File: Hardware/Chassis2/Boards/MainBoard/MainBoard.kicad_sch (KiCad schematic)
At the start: 28 parts, among them J1 Conn_02x08_Counter_Clockwise, J11 Conn_02x10_Counter_Clockwise, J12 Conn_02x10_Counter_Clockwise, J13 Conn_02x10_Counter_Clockwise, J14 Conn_02x10_Counter_Clockwise, J2 Conn_02x08_Counter_Clockwise, J3 Conn_02x08_Counter_Clockwise, J4 TBP01R1-508-06BE, J5 Conn_02x10_Counter_Clockwise, J6 TBP01R2-508-06BE

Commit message: Added New Control Board
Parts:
- removed C148, C149, C150, C151, C152, C153, C154, C155, C156, C157, C158, C159: UCM1H101MCL1GS, InverterCom:CAPAE660X800N, symbol InverterCom:UCM1H101MCL1GS
- removed H1, H7: MountingHole, MountingHole:MountingHole_3.2mm_M3, symbol Mechanical:MountingHole
- removed H3, H4, H5, H8: MountingHole, MountingHole:MountingHole_4.3mm_M4, symbol Mechanical:MountingHole
- removed J1, J2, J3: Conn_02x08_Counter_Clockwise, Connector_PinSocket_2.54mm:PinSocket_2x08_P2.54mm_Vertical, symbol Connector_Generic:Conn_02x08_Counter_Clockwise
- removed J11, J12, J13, J14, J5: Conn_02x10_Counter_Clockwise, Connector_PinHeader_2.54mm:PinHeader_2x10_P2.54mm_Vertical, symbol Connector_Generic:Conn_02x10_Counter_Clockwise
- removed J4: TBP01R1-508-06BE, InverterCom:TBP01R150806BE, symbol InverterCom:TBP01R1-508-06BE
- removed J6: TBP01R2-508-06BE, InverterCom:TBP01R250806BE, symbol InverterCom:TBP01R2-508-06BE
- added D3, D4: S3N, InverterCom:DIOM8059X265N, symbol InverterCom:S3N
- added F1: MF-RHT200_32-2, InverterCom:MFRHT200322, symbol InverterCom:MF-RHT200_32-2
- added J6: 776231-1, 7762311, symbol InverterCom:776231-1
- added PS3: EC7BW-110S12, EC7BW110S12, symbol InverterCom:EC7BW-110S12
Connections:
- net CAN_HIGH: now also J6.16
- net CAN_JUMPER_A: now also J6.2
- net CAN_LOW: now also J6.24, J6.27
- net GND_A: now also J6.15, PS3.5 (-VOUT)
- new net: D3.2 (A), D4.2 (A), F1.2
- new net +12V_OUT_A: PS3.3 (+VOUT)
- new net +5V_A: J6.26
- new net DIGITAL_IN_1: J6.18
- new net DIGITAL_IN_2: J6.30
- new net DIGITAL_IN_8: J6.21
- new net GND_Z: PS3.2 (-VIN)
- new net MOTOR_TMP_SENSE_IN: J6.33
- new net THROTTLE_A_IN: J6.22
- new net THROTTLE_B_IN: J6.23
- new net VIN_FUSED_Z: D3.1 (K), D4.1 (K), PS3.1 (+VIN)
- new net VIN_Z: F1.1, J6.1, J6.6
- no-connect marks 0 -> 20
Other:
- removed sheet ADC_1
- removed sheet CAN
- removed sheet OutputRelays
- note added: "+12V POWER SUPPLY 15W MAX"
- note added: "INPUT POLARITY PROTECTION"
- note added: "VIN IS 9-18V ONLY"
- note removed: "CANBUS OUTPUT CONNECTOR TO CONTROL BOARD INTERFACES TO OUTSIDE WORLD"
- note removed: "CONNECTION FROM MAINBOARD TO CONTROL MODULE ABOVE PROVIDES RELAY OUTPUTS + GATE DRIVER INTERLOCK"
- note removed: "CONNECTOR FROM MAIN BOARD TO CONTROL MODULE ABOVE ADC SPI INPUTS / POWER TO ADCS"
- note removed: "CONNECTOR FROM MAIN BOARD TO CONTROL MODULE ABOVE ADC SPI INPUTS / POWER TO ADCS / GATE DRIVE SIGNALS"
- note removed: "CONNECTOR FROM MAIN BOARD TO CONTROL MODULE ABOVE CONTROL INPUTS + POWER TO RELAY SUBSYSTEM/GATE DRIVERS"
- note removed: "CONNECTOR FROM THIS CONTROL BOARD TO GATE DRIVER ABOVE"

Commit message: Finished New Control Board, Did Schematic For Interface Board
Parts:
- added J1: TBP01R2W-508-06BE, SHDR6W100P0X508_1X6_4064X850X1240P, symbol InverterCom:TBP01R2W-508-06BE
- added J10, J13: Conn_02x03_Counter_Clockwise, Connector_PinHeader_2.54mm:PinHeader_2x03_P2.54mm_Vertical, symbol Connector_Generic:Conn_02x03_Counter_Clockwise
- added J12, J7: Conn_02x08_Counter_Clockwise, Connector_PinHeader_2.54mm:PinHeader_2x08_P2.54mm_Vertical, symbol Connector_Generic:Conn_02x08_Counter_Clockwise
- added J14: Conn_01x10, Connector_PinHeader_2.54mm:PinHeader_1x10_P2.54mm_Vertical, symbol Connector_Generic:Conn_01x10
- added J2: Conn_01x02, Connector_PinHeader_2.54mm:PinHeader_1x02_P2.54mm_Vertical, symbol Connector_Generic:Conn_01x02
- added R1, R3, R4, R5, R6, R82: 47k, Resistor_SMD:R_1210_3225Metric_Pad1.30x2.65mm_HandSolder, symbol Device:R
- added R2, R7: 10k, Resistor_SMD:R_1210_3225Metric_Pad1.30x2.65mm_HandSolder, symbol Device:R
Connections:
- net +12V_OUT_A: now also J2.1 (Pin_1)
- net +5V_A: now also J7.16 (Pin_16)
- net CAN_JUMPER_B: now also J6.24
- net DIGITAL_IN_1: now also R3.2
- net DIGITAL_IN_2: now also R4.2
- net GND_A: now also J2.2 (Pin_2), J7.10 (Pin_10), J7.12 (Pin_12), J7.13 (Pin_13), J7.14 (Pin_14), J7.15 (Pin_15), J7.2 (Pin_2), J7.4 (Pin_4), J7.6 (Pin_6), J7.8 (Pin_8)
- net GND_Z: now also J1.1, R6.1, R82.1
- net THROTTLE_A_IN: now also J7.9 (Pin_9)
- net THROTTLE_B_IN: now also J7.11 (Pin_11)
- net VIN_Z: now also R1.2, R5.2
- net CAN1_+5V: now reaches J6.28
- net CAN1_+5V: now also J10.3 (Pin_3)
- net ENCODER_COS: now reaches J6.35
- net ENCODER_COS: now also J7.3 (Pin_3)
- net CAN_HIGH renamed CAN1_HIGH
- net CAN1_HIGH: now also J10.6 (Pin_6)
- net CAN_LOW renamed CAN1_LOW
- net CAN1_LOW: now also J10.5 (Pin_5); no longer J6.24
- net DIGITAL_IN_8 renamed ENCODER_SIN
- net ENCODER_SIN: now also J7.1 (Pin_1)
- net MOTOR_TMP_SENSE_IN renamed MOTOR_TEMP_IN
- net MOTOR_TEMP_IN: now also J7.7 (Pin_7)
- new net: R4.1, R5.1, R6.2, R7.2
- new net: R1.1, R2.2, R3.1, R82.2
- new net CAN1_GND: J10.4 (Pin_4)
- new net CAN1_JUMPER_A: J10.1 (Pin_1)
- new net CAN1_JUMPER_B: J10.2 (Pin_2)
- new net CAN2_+5V: J1.6, J13.3 (Pin_3)
- new net CAN2_GND: J1.3, J13.4 (Pin_4)
- new net CAN2_HIGH: J1.5, J13.6 (Pin_6)
- new net CAN2_JUMPER_A: J13.1 (Pin_1)
- new net CAN2_JUMPER_B: J13.2 (Pin_2)
- new net CAN2_LOW: J1.4, J13.5 (Pin_5)
- new net DIN_1_W: J12.1 (Pin_1), R2.1
- new net DIN_2_W: J12.3 (Pin_3), R7.1
- new net DIN_3_W: J12.5 (Pin_5)
- new net DIN_4_W: J12.7 (Pin_7)
- new net DIN_5_W: J12.9 (Pin_9)
- new net DIN_6_W: J12.11 (Pin_11)
- new net DIN_7_W: J12.13 (Pin_13)
- new net DIN_8_W: J12.15 (Pin_15)
- new net GND_W: J12.10 (Pin_10), J12.12 (Pin_12), J12.14 (Pin_14), J12.16 (Pin_16), J12.2 (Pin_2), J12.4 (Pin_4), J12.6 (Pin_6), J12.8 (Pin_8)
- new net HALL_W_IN: J7.5 (Pin_5)
- no-connect marks 20 -> 36
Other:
- note added: "CONNECT PIN 1 TO BATT- WHEN RUNNING FOR REAL"
- note added: "Connector to IO board"
- note added: "SINGLE WIRE DEBUG / PROGRAMMING"
- note added: "passthrough, leave above board below, we can simply add a female to male header with long pins here to make probing easier"
- note added: "power out to board below us"
- note added: "vdivs for digital inputs"
- note removed: "+12V POWER SUPPLY 15W MAX"
- note removed: "VIN IS 9-18V ONLY"
- moved on the sheet: J6

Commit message: Add New Mainboard
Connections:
- net GND_W: now also J1.2
- no-connect marks 36 -> 35
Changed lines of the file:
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@@
-	)
-	(no_connect
-		(at 151.13 30.48)
 	)
 	(no_connect
@@
 		(effects
 			(font
+				(size 1.27 1.27)
+			)
+			(justify right bottom)
+		)
+	)
+	(label "GND_W"
+		(at 151.13 30.48 270)
+		(effects
+			(font

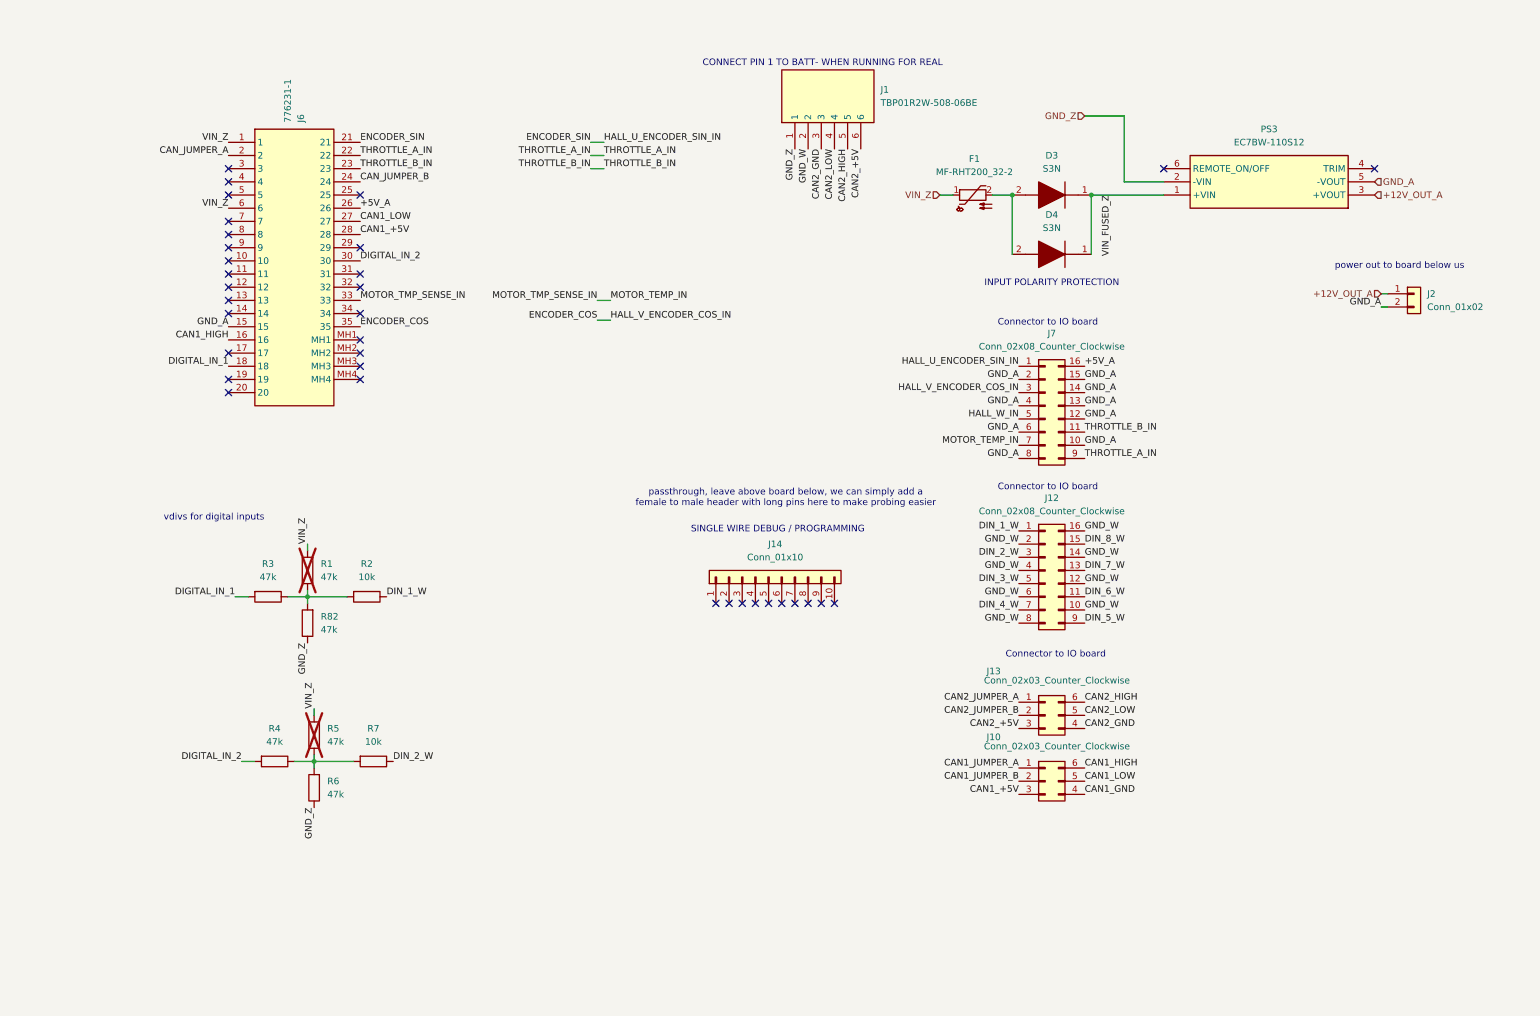
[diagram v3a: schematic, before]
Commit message: Update Inverter design for powertrain integration
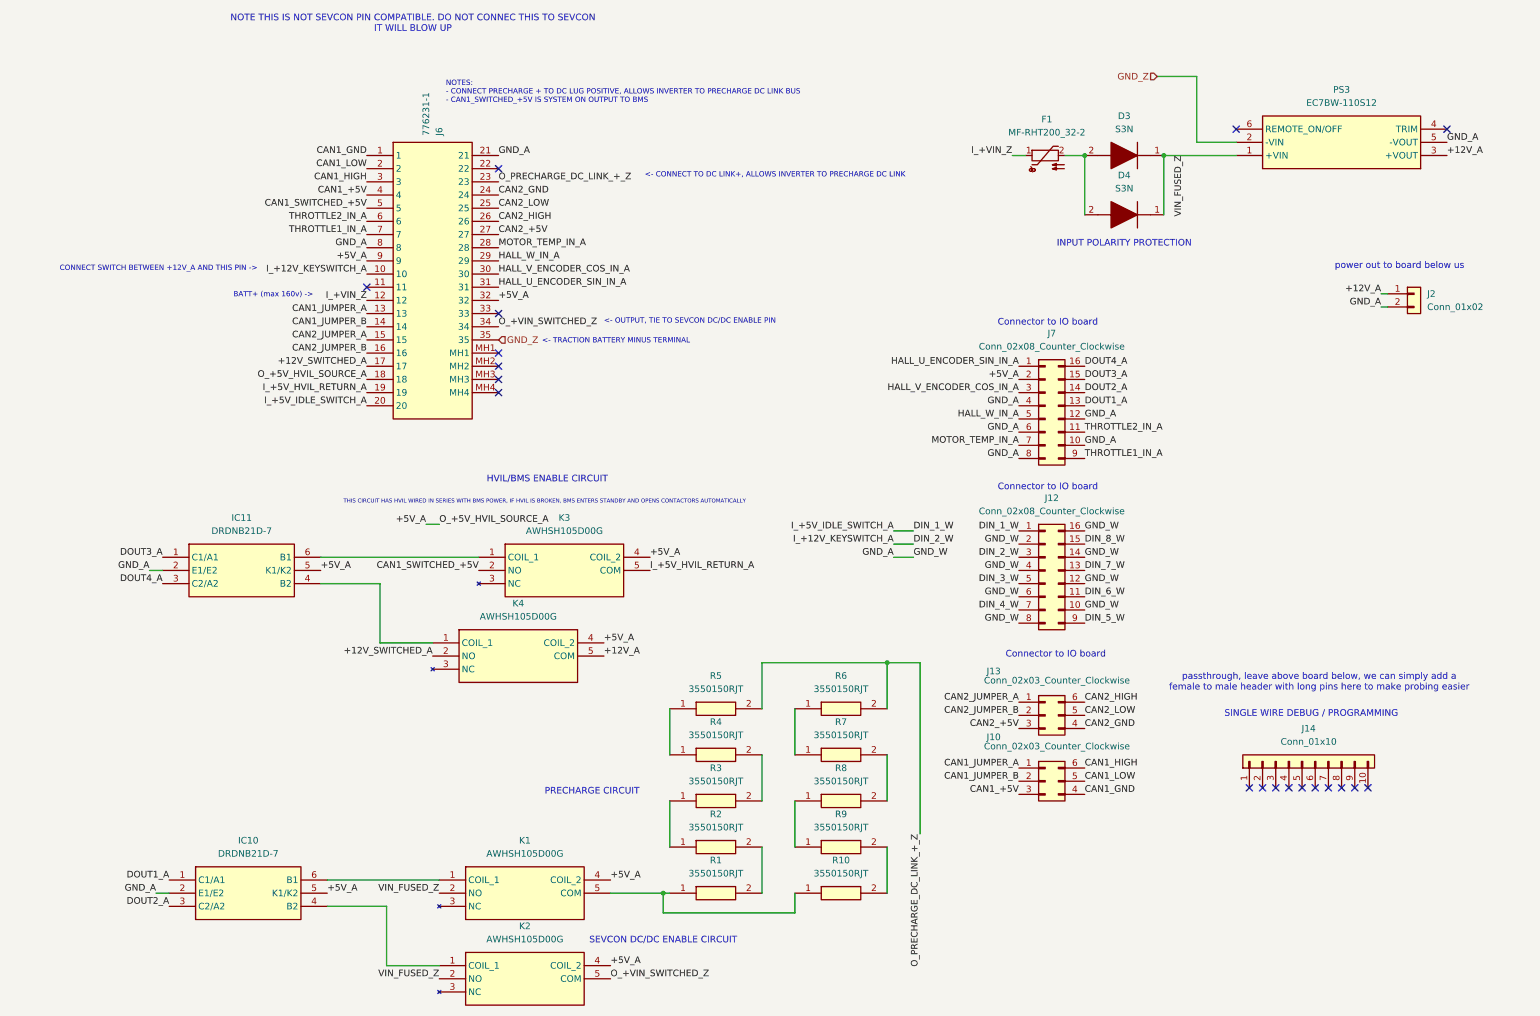
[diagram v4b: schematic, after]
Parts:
- removed J1: TBP01R2W-508-06BE, SHDR6W100P0X508_1X6_4064X850X1240P, symbol InverterCom:TBP01R2W-508-06BE
- removed R1, R3, R4, R5, R6, R82: 47k, Resistor_SMD:R_1210_3225Metric_Pad1.30x2.65mm_HandSolder, symbol Device:R
- removed R2, R7: 10k, Resistor_SMD:R_1210_3225Metric_Pad1.30x2.65mm_HandSolder, symbol Device:R
- added IC10, IC11: DRDNB21D-7, InverterCom:SOT65P210X110-6N, symbol InverterCom:DRDNB21D-7
- added K1, K2, K3, K4: AWHSH105D00G, InverterCom:AWHSH105D00G, symbol InverterCom:AWHSH105D00G
- added R1, R10, R2, R3, R4, R5, R6, R7, R8, R9: 3550150RJT, RESC11050X120N, symbol InverterCom:3550150RJT
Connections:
- net CAN_JUMPER_A is gone; now on net CAN1_LOW: J6.2
- net CAN_JUMPER_B is gone; now on net CAN2_GND: J6.24
- net DIGITAL_IN_1 is gone; now on net +5V_A: J6.18
- net GND_W is gone; now on net GND_A: J12.10 (Pin_10), J12.12 (Pin_12), J12.14 (Pin_14), J12.16 (Pin_16), J12.2 (Pin_2), J12.4 (Pin_4), J12.6 (Pin_6), J12.8 (Pin_8)
- net HALL_W_IN is gone; now on net HALL_W_IN_A: J7.5 (Pin_5)
- net +5V_A: now also J6.32, J6.9, J7.2 (Pin_2), IC10.5 (K1/K2), IC11.5 (K1/K2), K1.4 (COIL_2), K2.4 (COIL_2), K3.4 (COIL_2), K4.4 (COIL_2); no longer J6.26, J7.16 (Pin_16)
- net CAN1_+5V: now also J6.4; no longer J6.28
- net CAN1_GND: now also J6.1
- net CAN1_HIGH: now also J6.3; no longer J6.16
- net CAN1_JUMPER_A: now also J6.13
- net CAN1_JUMPER_B: now also J6.14
- net CAN1_LOW: no longer J6.27
- net CAN2_+5V: now also J6.27
- net CAN2_HIGH: now also J6.26
- net CAN2_JUMPER_A: now also J6.15
- net CAN2_JUMPER_B: now also J6.16
- net CAN2_LOW: now also J6.25
- net DIN_1_W: now also J6.20
- net DIN_2_W: now also J6.10
- net GND_A: now also J6.21, J6.8, IC10.2 (E1/E2), IC11.2 (E1/E2); no longer J6.15, J7.13 (Pin_13), J7.14 (Pin_14), J7.15 (Pin_15), J7.2 (Pin_2)
- net GND_Z: now also J6.35
- net VIN_FUSED_Z: now also K1.2 (NO), K2.2 (NO)
- net I_+VIN_Z: now reaches J6.12
- net I_+VIN_Z: now also F1.1
- net +12V_SWITCHED_A: now reaches J6.17
- net +12V_SWITCHED_A: now also K4.2 (NO)
- net I_+5V_HVIL_RETURN_A: now reaches J6.19
- net I_+5V_HVIL_RETURN_A: now also K3.5 (COM)
- net HALL_W_IN_A: now reaches J6.29
- net HALL_U_ENCODER_SIN_IN_A: now reaches J6.31
- net HALL_U_ENCODER_SIN_IN_A: now also J7.1 (Pin_1)
- net O_+VIN_SWITCHED_Z: now reaches J6.34
- net O_+VIN_SWITCHED_Z: now also K2.5 (COM)
- net CAN1_SWITCHED_+5V: now reaches J6.5
- net CAN1_SWITCHED_+5V: now also K3.2 (NO)
- net THROTTLE1_IN_A: now reaches J6.7
- net THROTTLE1_IN_A: now also J7.9 (Pin_9)
- net +12V_OUT_A renamed +12V_A
- net +12V_A: now also K4.5 (COM)
- net DIGITAL_IN_2 renamed HALL_V_ENCODER_COS_IN_A
- net HALL_V_ENCODER_COS_IN_A: now also J7.3 (Pin_3)
- removed net ENCODER_COS: J6.35, J7.3 (Pin_3)
- removed net ENCODER_SIN: J6.21, J7.1 (Pin_1)
- net MOTOR_TEMP_IN: no longer names the net of J6.33
- net MOTOR_TEMP_IN: no longer J7.7 (Pin_7)
- net THROTTLE_A_IN: no longer names the net of J6.22
- net THROTTLE_A_IN: no longer J7.9 (Pin_9)
- net THROTTLE_B_IN renamed O_PRECHARGE_DC_LINK_+_Z
- net O_PRECHARGE_DC_LINK_+_Z: now also R5.2, R6.2; no longer J7.11 (Pin_11)
- removed net VIN_Z: F1.1, J6.1, J6.6
- new net: R6.1, R7.1
- new net: R4.1, R5.1
- new net: R3.2, R4.2
- new net: IC10.4 (B2), K2.1 (COIL_1)
- new net: IC10.6 (B1), K1.1 (COIL_1)
- new net: R8.1, R9.1
- new net: R10.2, R9.2
- new net: K1.5 (COM), R1.1, R10.1
- new net: R7.2, R8.2
- new net: R2.1, R3.1
- new net: R1.2, R2.2
- new net: IC11.6 (B1), K3.1 (COIL_1)
- new net: IC11.4 (B2), K4.1 (COIL_1)
- new net DOUT1_A: IC10.1 (C1/A1), J7.13 (Pin_13)
- new net DOUT2_A: IC10.3 (C2/A2), J7.14 (Pin_14)
- new net DOUT3_A: IC11.1 (C1/A1), J7.15 (Pin_15)
- new net DOUT4_A: IC11.3 (C2/A2), J7.16 (Pin_16)
- new net MOTOR_TEMP_IN_A: J6.28, J7.7 (Pin_7)
- new net THROTTLE2_IN_A: J6.6, J7.11 (Pin_11)
- no-connect marks 35 -> 19
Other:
- note added: "<- CONNECT TO DC LINK+, ALLOWS INVERTER TO PRECHARGE DC LINK"
- note added: "<- OUTPUT, TIE TO SEVCON DC/DC ENABLE PIN"
- note added: "<- TRACTION BATTERY MINUS TERMINAL"
- note added: "BATT+ (max 160v) ->"
- note added: "CONNECT SWITCH BETWEEN +12V_A AND THIS PIN ->"
- note added: "HVIL/BMS ENABLE CIRCUIT"
- note added: "NOTE THIS IS NOT SEVCON PIN COMPATIBLE. DO NOT CONNEC THIS TO SEVCON IT WILL BLOW UP"
- note added: "NOTES: - CONNECT PRECHARGE + TO DC LUG POSITIVE, ALLOWS INVERTER TO PRECHARGE DC LINK BUS - CAN1_SWITCHED_+5V IS SYSTEM ON OUTPUT TO BMS"
- note added: "PRECHARGE CIRCUIT"
- note added: "SEVCON DC/DC ENABLE CIRCUIT"
- note added: "THIS CIRCUIT HAS HVIL WIRED IN SERIES WITH BMS POWER, IF HVIL IS BROKEN, BMS ENTERS STANDBY AND OPENS CONTACTORS AUTOMATICALLY"
- note removed: "CONNECT PIN 1 TO BATT- WHEN RUNNING FOR REAL"
- note removed: "vdivs for digital inputs"
- moved on the sheet: D3, D4, F1, J14, J6, PS3

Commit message: Added FRAM chip to inverter
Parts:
- added C187, C188, C189: 100nF, Capacitor_SMD:C_1210_3225Metric_Pad1.33x2.70mm_HandSolder, symbol Device:C
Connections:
- net +12V_A: now also C189.2
- net +5V_A: now also C187.2, C188.2; no longer J6.18
- net CAN1_+5V: now also J6.18
- net GND_A: now also C187.1, C188.1, C189.1
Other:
- note added: "+5V HVIL OUTPUT, IN SERIES WITH SYS ON TO BMS ->"
- note added: "+5V HVIL RETURN, IN SERIES WITH SYS ON TO BMS ->"
- note added: "<- DASH, CHARGER, ABS CANBUS +5V"
- note added: "<- DASH, CHARGER, ABS CANBUS GND"
- note added: "<- DASH, CHARGER, ABS CANBUS HIGH"
- note added: "<- DASH, CHARGER, ABS CANBUS LOW"
- note added: "<- GND REFERENCE FOR MOTOR TMP, ENCODER"
- note added: "<- MOTOR ENCODER/TMP SENSOR +5V"
- note added: "<- MOTOR HALL U OR ENCODER SIN (DEPENDING ON SENSOR TYPE)"
- note added: "<- MOTOR HALL V OR ENCODER COSINE (DEPENDING ON SENSOR TYPE)"
- note added: "<- MOTOR HALL W (IF USED, IF SIN/COS LEAVE N/C)"
- note added: "<- MOTOR THERMISTOR (TIE OTHER END OF THERMISTOR TO GND_A)"
- note added: "AUX 12V OUT, TO DISPLAY, KEYSWITCH ->"
- note added: "BLANK TO ISOLATE TRACTION BATTERY VOLTAGE ->"
- note added: "BMS CAN1 +5V ->"
- note added: "BMS CAN1 GND ->"
- note added: "BMS CAN1 HIGH ->"
- note added: "BMS CAN1 LOW ->"
- note added: "CAN1 TERMINATION JUMPER ->"
- note added: "CAN2 TERMINATION JUMPER ->"
- note added: "REDUNDANT THROTTLE A INPUT ->"
- note added: "REDUNDANT THROTTLE B INPUT ->"
- note added: "SYSTEM ON REF TO BMS->"
- note added: "THROTTLE +5V ->"
- note added: "THROTTLE GROUND ->"
- note added: "THROTTLE HOME POSITION SWITCH (REF'D TO THROTTLE +5V) ->"
- note added: "TRACTION BATT+ (max 160v) ->"
- note removed: "BATT+ (max 160v) ->"
- note removed: "NOTES: - CONNECT PRECHARGE + TO DC LUG POSITIVE, ALLOWS INVERTER TO PRECHARGE DC LINK BUS - CAN1_SWITCHED_+5V IS SYSTEM ON OUTPUT TO BMS"
- moved on the sheet: D3, D4, F1, J14, J2, J6, J7

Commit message: Finish New control board
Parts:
- added C36, C37, C38, C39, C40, C41, C42, C43, C44, C45, C46, C47, C48, C49, C50, C51: UCM1H101MCL1GS, CAPAE660X800N, symbol InverterCom:UCM1H101MCL1GS
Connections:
- net +12V_A: now also C42.1 (+), C43.1 (+), C44.1 (+), C45.1 (+), C46.1 (+), C47.1 (+), C48.1 (+), C49.1 (+), C50.1 (+), C51.1 (+)
- net +5V_A: now also C36.1 (+), C37.1 (+), C38.1 (+), C39.1 (+), C40.1 (+), C41.1 (+)
- net GND_A: now also C36.2 (-), C37.2 (-), C38.2 (-), C39.2 (-), C40.2 (-), C41.2 (-), C42.2 (-), C43.2 (-), C44.2 (-), C45.2 (-), C46.2 (-), C47.2 (-), C48.2 (-), C49.2 (-), C50.2 (-), C51.2 (-)
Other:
- moved on the sheet: C189

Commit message: forgot
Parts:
- removed R5, R6: 3550150RJT, RESC11050X120N, symbol InverterCom:3550150RJT
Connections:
- net O_PRECHARGE_DC_LINK_+_Z: now also R4.1, R7.1

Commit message: Display sorta working
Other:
- note added: "Unfuck these they're switched."
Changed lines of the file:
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@@
+		)
+	)
+	(text "Unfuck these they're switched."
+		(exclude_from_sim no)
+		(at 33.274 97.79 0)
+		(effects
+			(font
+				(size 1.27 1.27)
+			)
 		)
 	)
